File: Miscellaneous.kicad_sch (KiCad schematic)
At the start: 12 parts

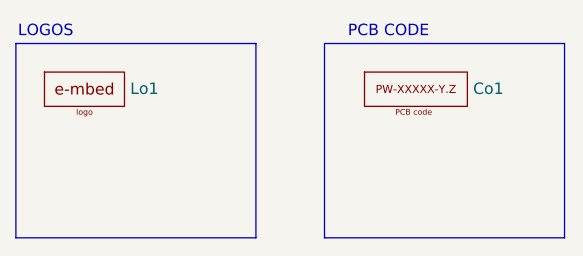
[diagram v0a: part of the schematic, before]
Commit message: Local library added
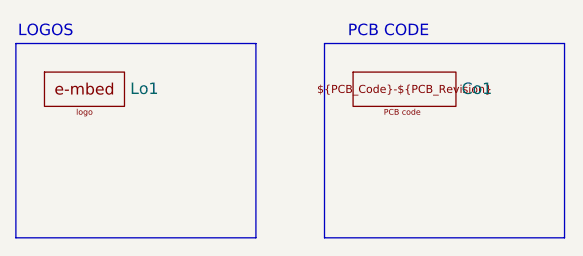
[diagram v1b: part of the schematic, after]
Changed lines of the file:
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@@
 	)
 	(symbol
-		(lib_name "PCBCode_1")
 		(lib_id "e-mbedLocalLib:PCBCode")
-		(at 153.67 16.51 0)
+		(at 152.4 16.51 0)
 		(unit 1)
 		(exclude_from_sim no)
@@
 		(fields_autoplaced yes)
 		(property "Reference" "Co1"
-			(at 160.02 16.4478 0)
+			(at 158.75 16.4478 0)
 			(effects
 				(font
@@
 		)
 		(property "Value" "~"
-			(at 160.02 18.3529 0)
+			(at 158.75 18.3529 0)
 			(effects
 				(font
@@
 		)
 		(property "Footprint" "e-mbedLocalLib:PCBCodeCopper"
-			(at 153.67 16.51 0)
+			(at 152.4 16.51 0)
 			(effects
 				(font
@@
 		)
 		(property "Datasheet" ""
-			(at 153.67 16.51 0)
+			(at 152.4 16.51 0)
 			(effects
 				(font
@@
 		)
 		(property "Description" ""
-			(at 153.67 16.51 0)
+			(at 152.4 16.51 0)
 			(effects
 				(font
